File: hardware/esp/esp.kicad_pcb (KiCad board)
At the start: 2 copper layers, 100 x 80 mm, 7 parts, among them J1 USB_C_Receptacle_USB2.0_16P, U1 BME280, U2 VL53L0X, U3 NRF24L01, U4 ESP32-S3-WROOM-1, U5 NT3H1101W0FHK

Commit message: Updating PCb and esp board schematics
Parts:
- removed the U3 at (114.0, 140.1)
- added C1: 10nF, Capacitor_SMD:C_0603_1608Metric, F.Cu at (170.9, 89.4)
- added C11: 1pF, Capacitor_SMD:C_0603_1608Metric, F.Cu at (181.9, 91.7)
- added C12: 0.1µF, Capacitor_SMD:C_0805_2012Metric, F.Cu at (148.3, 135.9)
- added C13: C, Capacitor_SMD:C_0603_1608Metric, F.Cu at (98.2, 86.0)
- added C14: 100nF, Capacitor_SMD:C_0603_1608Metric, F.Cu at (115.4, 138.5)
- added C15: C, Capacitor_SMD:C_0603_1608Metric, F.Cu at (91.8, 89.0)
- added C16: 4.7pF, Capacitor_SMD:C_0603_1608Metric, F.Cu at (103.2, 141.5)
- added C2: 1nF, Capacitor_SMD:C_0603_1608Metric, F.Cu at (162.9, 100.7)
- added C3: 33nF, Capacitor_SMD:C_0603_1608Metric, F.Cu at (167.9, 102.7)
- added C4: 22pF, Capacitor_SMD:C_0603_1608Metric, F.Cu at (175.9, 110.2)
- added C5: 2.2pF, Capacitor_SMD:C_0603_1608Metric, F.Cu at (176.9, 103.7)
- added C7: 22pF, Capacitor_SMD:C_0603_1608Metric, F.Cu at (182.9, 103.7)
- added C8: 4.7pF, Capacitor_SMD:C_0603_1608Metric, F.Cu at (176.9, 90.4)
- added C9: 1.5pF, Capacitor_SMD:C_0603_1608Metric, F.Cu at (180.9, 80.4)
- added L2: 8.2nH, Inductor_SMD:L_0603_1608Metric, F.Cu at (168.9, 83.4)
- added L3: 2.7nH, Inductor_SMD:L_0603_1608Metric, F.Cu at (171.4, 83.4)
- added L4: 2.7nH, Inductor_SMD:L_0603_1608Metric, F.Cu at (173.9, 83.4)
- added R10: 10K, Resistor_SMD:R_0805_2012Metric, F.Cu at (148.3, 132.9)
- added R16: 1.5K, Resistor_SMD:R_0805_2012Metric, F.Cu at (108.1, 142.5)
- added R17: 1.5K, Resistor_SMD:R_0805_2012Metric, F.Cu at (105.2, 132.5)
- added R18: 1.5K, Resistor_SMD:R_0805_2012Metric, F.Cu at (102.2, 136.5)
- added R19: R, Resistor_SMD:R_0805_2012Metric, F.Cu at (101.9, 80.0)
- added R20: 1.5K, Resistor_SMD:R_0805_2012Metric, F.Cu at (113.1, 131.5)
- added R21: R, Resistor_SMD:R_0805_2012Metric, F.Cu at (88.0, 76.0)
- added R22: R, Resistor_SMD:R_0805_2012Metric, F.Cu at (96.1, 74.0)
- added R3: 22K, Resistor_SMD:R_0603_1608Metric, F.Cu at (168.9, 108.6)
- added R4: 22R, Resistor_SMD:R_0805_2012Metric, F.Cu at (96.9, 118.0)
- added R5: 22R, Resistor_SMD:R_0805_2012Metric, F.Cu at (103.0, 122.0)
- added R6: 5.1k, Resistor_SMD:R_0805_2012Metric, F.Cu at (103.1, 117.0)
- added R7: 5.1k, Resistor_SMD:R_0805_2012Metric, F.Cu at (97.0, 123.0)
- added R8: 1M, Resistor_SMD:R_0805_2012Metric, F.Cu at (180.9, 115.3)
- added R9: 10k, Resistor_SMD:R_0805_2012Metric, F.Cu at (148.3, 130.0)
- added SW1: RESET, Button_Switch_SMD:SW_SPST_SKQG_WithStem, F.Cu at (107.0, 97.0)
- added SW2: BOOT, Button_Switch_SMD:SW_SPST_SKQG_WithStem, F.Cu at (155.0, 116.0)
- added U2: NRF24L01, Package_DFN_QFN:QFN-20-1EP_4x4mm_P0.5mm_EP2.5x2.5mm, F.Cu at (168.9, 97.5)
- added Y1: 16MHz, Crystal:Crystal_SMD_3225-4Pin_3.2x2.5mm, F.Cu at (175.9, 97.4)
- moved U4 60.0 mm to (109.8, 137.0)
- moved J1 8.89 mm to (88.0, 120.1)
- renumbered U5 to U1, U4 to U3, U2 to U4, U1 to U5
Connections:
- J1 pad A5: unconnected-(J1-CC1-PadA5) -> Net-(J1-CC1)
- J1 pad B5: unconnected-(J1-CC2-PadB5) -> Net-(J1-CC2)
- U1 pad 2: unconnected-(U5-VSS-Pad2) -> GND
- U1 pad 3: unconnected-(U5-SCL-Pad3) -> SCL
- U1 pad 4: unconnected-(U5-FD-Pad4) -> NFC_FD
- U1 pad 5: unconnected-(U5-SDA-Pad5) -> SDA
- U1 pad 6: unconnected-(U5-VCC-Pad6) -> +3V3
- U3 pad 1: Net-(U4-GND-Pad1) -> GND
- U3 pad 12: unconnected-(U4-IO8-Pad12) -> SDA
- U3 pad 15: unconnected-(U4-IO3-Pad15) -> C.SKULL
- U3 pad 17: unconnected-(U4-IO9-Pad17) -> SCL
- U3 pad 2: unconnected-(U4-3V3-Pad2) -> +3V3
- U3 pad 27: unconnected-(U4-IO0-Pad27) -> BOOT
- U3 pad 3: unconnected-(U4-EN-Pad3) -> EN
- U3 pad 38: unconnected-(U4-IO2-Pad38) -> O.SKULL
- U3 pad 39: unconnected-(U4-IO1-Pad39) -> NRFLED
- U3 pad 4: unconnected-(U4-IO4-Pad4) -> NF.SKULL
- U3 pad 40: Net-(U4-GND-Pad1) -> GND
- U3 pad 41: Net-(U4-GND-Pad1) -> GND
- U3 pad 5: unconnected-(U4-IO5-Pad5) -> NFCLED
- U4 pad 1: unconnected-(U2-AVDDVCSEL-Pad1) -> +3V3
- U4 pad 10: unconnected-(U2-SCL-Pad10) -> SCL
- U4 pad 11: unconnected-(U2-AVDD-Pad11) -> +3V3
- U4 pad 2: unconnected-(U2-AVSSVCSEL-Pad2) -> GND
- U4 pad 5: unconnected-(U2-~{XSHUT}-Pad5) -> XSHUT
- U4 pad 7: unconnected-(U2-GPIO1-Pad7) -> DIST_GPIO1
- U4 pad 9: unconnected-(U2-SDA-Pad9) -> SDA
- U5 pad 1: unconnected-(U1-GND-Pad1) -> GND
- U5 pad 2: unconnected-(U1-CSB-Pad2) -> Net-(U5-CSB)
- U5 pad 3: unconnected-(U1-SDI-Pad3) -> SDA
- U5 pad 4: unconnected-(U1-SCK-Pad4) -> SCL
- U5 pad 6: unconnected-(U1-VDDIO-Pad6) -> +3V3
- U5 pad 7: unconnected-(U1-GND-Pad7) -> GND
- U5 pad 8: unconnected-(U1-VDD-Pad8) -> +3V3

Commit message: Updating schematics and PCB
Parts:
- removed L4: 2.7nH, Inductor_SMD:L_0603_1608Metric
- added C10: 33nF, Capacitor_SMD:C_0603_1608Metric, F.Cu at (34.0, 146.4)
- added C17: 1.5pF, Capacitor_SMD:C_0603_1608Metric, F.Cu at (38.0, 148.9)
- added C18: 1pF, Capacitor_SMD:C_0603_1608Metric, F.Cu at (38.0, 151.4)
- added C19: C, Capacitor_SMD:C_0603_1608Metric, F.Cu at (38.0, 154.0)
- added C20: C, Capacitor_SMD:C_0603_1608Metric, F.Cu at (42.0, 141.4)
- added C6: 0.1µF, Capacitor_SMD:C_0805_2012Metric, F.Cu at (29.7, 136.1)
- added D1: LED, LED_SMD:LED_0603_1608Metric, F.Cu at (63.3, 120.8)
- added D2: LED, LED_SMD:LED_0603_1608Metric, F.Cu at (63.3, 123.4)
- added D3: LED, LED_SMD:LED_0603_1608Metric, F.Cu at (63.3, 126.0)
- added D4: LED, LED_SMD:LED_0603_1608Metric, F.Cu at (63.3, 128.6)
- added D5: LED, LED_SMD:LED_0603_1608Metric, F.Cu at (63.3, 131.2)
- added D6: LED, LED_SMD:LED_0603_1608Metric, F.Cu at (63.3, 133.7)
- added D7: LED, LED_SMD:LED_0603_1608Metric, F.Cu at (63.3, 136.3)
- added G***: LOGO, LOGO, F.Cu at (179.0, 133.0)
- added G***: LOGO, LOGO, F.Cu at (169.0, 141.0)
- added J2: Conn_01x02, Connector_PinHeader_2.54mm:PinHeader_1x02_P2.54mm_Vertical, F.Cu at (139.0, 72.5)
- added J3: USB_C_Receptacle_USB2.0_16P, Connector_USB:USB_C_Receptacle_HCTL_HC-TYPE-C-16P-01A, F.Cu at (101.7, 72.1)
- added J4: Conn_01x01_Pin, Connector_PinHeader_1.00mm:PinHeader_1x01_P1.00mm_Vertical, F.Cu at (98.0, 116.0)
- added J5: Conn_01x09_Pin, Connector_PinHeader_2.54mm:PinHeader_1x09_P2.54mm_Vertical, F.Cu at (91.7, 105.0)
- added J6: Conn_01x09_Pin, Connector_PinHeader_2.54mm:PinHeader_1x09_P2.54mm_Vertical, F.Cu at (158.9, 105.0)
- added L1: 8.2nH, Inductor_SMD:L_0603_1608Metric, F.Cu at (42.0, 143.9)
- added R1: 22R, Resistor_SMD:R_0805_2012Metric, F.Cu at (34.2, 121.0)
- added R11: R, Resistor_SMD:R_0805_2012Metric, F.Cu at (38.6, 129.8)
- added R12: R, Resistor_SMD:R_0805_2012Metric, F.Cu at (38.6, 132.8)
- added R13: R, Resistor_SMD:R_0805_2012Metric, F.Cu at (38.6, 135.7)
- added R14: 1.5K, Resistor_SMD:R_0805_2012Metric, F.Cu at (38.6, 138.7)
- added R15: 1.5K, Resistor_SMD:R_0805_2012Metric, F.Cu at (43.0, 121.0)
- added R2: 22R, Resistor_SMD:R_0805_2012Metric, F.Cu at (34.2, 123.9)
- added R23: 22R, Resistor_SMD:R_0805_2012Metric, F.Cu at (47.4, 121.0)
- added R24: 22R, Resistor_SMD:R_0805_2012Metric, F.Cu at (47.4, 123.9)
- added R25: 5.1k, Resistor_SMD:R_0805_2012Metric, F.Cu at (47.4, 126.9)
- added R26: 5.1k, Resistor_SMD:R_0805_2012Metric, F.Cu at (47.4, 129.8)
- added U6: CP2102N-Axx-xQFN20, Package_DFN_QFN:SiliconLabs_QFN-20-1EP_3x3mm_P0.5mm_EP1.8x1.8mm, F.Cu at (101.8, 88.8)
- C1: value 10nF -> 10uF; footprint Capacitor_SMD:C_0603_1608Metric -> Capacitor_SMD:C_0805_2012Metric
- C11: value 1pF -> 100nF
- C12: value 0.1µF -> 22pF; footprint Capacitor_SMD:C_0805_2012Metric -> Capacitor_SMD:C_0603_1608Metric
- C13: value C -> 2.2pF
- C14: value 100nF -> 4.7pF
- C15: value C -> 22pF
- C2: value 1nF -> 0.1uF; footprint Capacitor_SMD:C_0603_1608Metric -> Capacitor_SMD:C_0805_2012Metric
- C3: value 33nF -> 10uF; footprint Capacitor_SMD:C_0603_1608Metric -> Capacitor_SMD:C_0805_2012Metric
- C4: value 22pF -> 0.1uF; footprint Capacitor_SMD:C_0603_1608Metric -> Capacitor_SMD:C_0805_2012Metric
- C5: value 2.2pF -> C; footprint Capacitor_SMD:C_0603_1608Metric -> Capacitor_SMD:C_0805_2012Metric
- C7: value 22pF -> C; footprint Capacitor_SMD:C_0603_1608Metric -> Capacitor_SMD:C_0805_2012Metric
- C8: value 4.7pF -> 10nF
- C9: value 1.5pF -> 1nF
- L2: value 8.2nH -> 2.7nH
- R10: value 10K -> R
- R16: value 1.5K -> 22K; footprint Resistor_SMD:R_0805_2012Metric -> Resistor_SMD:R_0603_1608Metric
- R19: value R -> 1M
- R20: value 1.5K -> R
- R3: value 22K -> 5.1k; footprint Resistor_SMD:R_0603_1608Metric -> Resistor_SMD:R_0805_2012Metric
- R4: value 22R -> 5.1k
- R5: value 22R -> R
- R6: value 5.1k -> 10k
- R7: value 5.1k -> 10K
- R8: value 1M -> R
- R9: value 10k -> R
- U1: value NT3H1101W0FHK -> AMS1117-3.3; footprint NT3H1101W0FHK:IC_NT3H1101W0FHK -> Package_TO_SOT_SMD:SOT-223-3_TabPin2
- U2: value NRF24L01 -> ESP32-S3-WROOM-1; footprint Package_DFN_QFN:QFN-20-1EP_4x4mm_P0.5mm_EP2.5x2.5mm -> RF_Module:ESP32-S3-WROOM-1
- U3: value ESP32-S3-WROOM-1 -> VL53L0X; footprint RF_Module:ESP32-S3-WROOM-1 -> VL53L0X:SENSOR_VL53L0X
- U4: value VL53L0X -> NRF24L01; footprint VL53L0X:SENSOR_VL53L0X -> Package_DFN_QFN:QFN-20-1EP_4x4mm_P0.5mm_EP2.5x2.5mm
- moved C9 160.1 mm to (34.0, 143.9), turned to 0 degrees
- moved C11 158.7 mm to (34.0, 148.9), turned to 0 degrees
- moved C7 157.2 mm to (29.7, 139.1), turned to 0 degrees
- moved C8 151.8 mm to (34.0, 141.4), turned to 0 degrees
- moved C5 150.1 mm to (29.7, 133.0), turned to 0 degrees
- moved C4 147.6 mm to (29.7, 130.0), turned to 0 degrees
- moved L3 145.1 mm to (42.0, 148.9), turned to 0 degrees
- moved C1 144.7 mm to (29.7, 121.0), turned to 0 degrees
- moved R8 142.5 mm to (38.6, 121.0), turned to 0 degrees
- moved L2 141.7 mm to (42.0, 146.4), turned to 0 degrees
- moved C3 140.3 mm to (29.7, 127.0), turned to 0 degrees
- moved R3 136.0 mm to (34.2, 126.9), turned to 0 degrees
- moved C2 135.2 mm to (29.7, 124.0), turned to 0 degrees
- moved C12 115.4 mm to (34.0, 151.4)
- moved R10 109.9 mm to (38.6, 126.9)
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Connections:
- C1 pad 1: GND -> +5V
- C1 pad 2: +3V3 -> GND
- C11 pad 1: GND -> +3V3
- C11 pad 2: Net-(C11-Pad2) -> GND
- C12 pad 2: EN -> Net-(U4-XC1)
- C13 pad 1: GND -> Net-(U4-VDD_PA)
- C13 pad 2: +3V3 -> GND
- C15 pad 1: +3V3 -> Net-(U4-XC2)
- C16 pad 1: +3V3 -> Net-(U4-VDD_PA)
- C2 pad 1: GND -> +5V
- C2 pad 2: +3V3 -> GND
- C3 pad 1: Net-(U2-DVDD) -> +3V3
- C4 pad 1: GND -> +3V3
- C4 pad 2: Net-(U2-XC1) -> GND
- C5 pad 1: Net-(U2-VDD_PA) -> GND
- C5 pad 2: GND -> +3V3
- C7 pad 1: Net-(U2-XC2) -> GND
- C7 pad 2: GND -> +3V3
- C8 pad 1: Net-(U2-VDD_PA) -> GND
- C8 pad 2: GND -> +3V3
- C9 pad 1: Net-(C9-Pad1) -> GND
- C9 pad 2: Net-(C11-Pad2) -> +3V3
- L2 pad 1: Net-(U2-ANT2) -> Net-(U4-ANT2)
- L2 pad 2: Net-(U2-ANT1) -> Net-(C17-Pad1)
- L3 pad 1: Net-(U2-ANT2) -> Net-(U4-ANT1)
- L3 pad 2: Net-(C9-Pad1) -> Net-(U4-VDD_PA)
- R10 pad 1: +3V3 -> NRFLED
- R10 pad 2: BOOT -> Net-(D4-A)
- R16 pad 1: +3V3 -> GND
- R16 pad 2: SDA -> Net-(U4-IREF)
- R17 pad 2: SCL -> XSHUT
- R18 pad 2: XSHUT -> DIST_GPIO1
- R19 pad 1: +3V3 -> Net-(U4-XC1)
- R19 pad 2: SDA -> Net-(U4-XC2)
- R20 pad 2: DIST_GPIO1 -> SDA
- R3 pad 1: GND -> Net-(J1-CC1)
- R3 pad 2: Net-(U2-IREF) -> GND
- R4 pad 1: Net-(J1-D--PadA7) -> Net-(J1-CC2)
- R4 pad 2: D- -> GND
- R5 pad 1: Net-(J1-D+-PadA6) -> Net-(D1-A)
- R5 pad 2: D+ -> +3V3
- R6 pad 1: Net-(J1-CC1) -> EN
- R6 pad 2: GND -> +3V3
- R7 pad 1: Net-(J1-CC2) -> +3V3
- R7 pad 2: GND -> BOOT
- R8 pad 1: Net-(U2-XC1) -> unconnected-(R8-Pad1)
- R8 pad 2: Net-(U2-XC2) -> Net-(D2-A)
- R9 pad 1: EN -> unconnected-(R9-Pad1)
- R9 pad 2: +3V3 -> Net-(D3-A)
- U1 pad 1: Net-(U1-LA) -> GND
- U1 pad 2: GND -> +3V3
- U1 pad 3: SCL -> +5V
- U2 pad 1: NRF_CE -> GND
- U2 pad 10: Net-(U2-XC1) -> unconnected-(U2-IO17-Pad10)
- U2 pad 11: Net-(U2-VDD_PA) -> unconnected-(U2-IO18-Pad11)
- U2 pad 12: Net-(U2-ANT1) -> SDA
- U2 pad 13: Net-(U2-ANT2) -> D-
- U2 pad 14: GND -> D+
- U2 pad 15: +3V3 -> C.SKULL
- U2 pad 16: Net-(U2-IREF) -> unconnected-(U2-IO46-Pad16)
- U2 pad 17: GND -> SCL
- U2 pad 18: +3V3 -> unconnected-(U2-IO10-Pad18)
- U2 pad 19: Net-(U2-DVDD) -> unconnected-(U2-IO11-Pad19)
- U2 pad 2: NRF_CSN -> +3V3
- U2 pad 21: (no net) -> unconnected-(U2-IO13-Pad21)
- U2 pad 3: SPI_SCK -> EN
- U2 pad 4: SPI_MOSI -> NF.SKULL
- U2 pad 5: SPI_MISO -> NFCLED
- U2 pad 7: +3V3 -> unconnected-(U2-IO7-Pad7)
- U2 pad 8: GND -> unconnected-(U2-IO15-Pad8)
- U2 pad 9: Net-(U2-XC2) -> unconnected-(U2-IO16-Pad9)
- U3 pad 1: GND -> +3V3
- U3 pad 10: unconnected-(U3-IO17-Pad10) -> SCL
- U3 pad 11: unconnected-(U3-IO18-Pad11) -> +3V3
- U3 pad 12: SDA -> GND
- U3 pad 2: +3V3 -> GND
- U3 pad 3: EN -> GND
- U3 pad 4: NF.SKULL -> GND
- U3 pad 5: NFCLED -> XSHUT
- U3 pad 6: unconnected-(U3-IO6-Pad6) -> GND
- U3 pad 7: unconnected-(U3-IO7-Pad7) -> DIST_GPIO1
- U3 pad 8: unconnected-(U3-IO15-Pad8) -> (no net)
- U3 pad 9: unconnected-(U3-IO16-Pad9) -> SDA
- U4 pad 1: +3V3 -> NRF_CE
- U4 pad 10: SCL -> Net-(U4-XC1)
- U4 pad 11: +3V3 -> Net-(U4-VDD_PA)
- U4 pad 12: GND -> Net-(U4-ANT1)
- U4 pad 2: GND -> NRF_CSN
- U4 pad 3: GND -> SPI_SCK
- U4 pad 4: GND -> SPI_MOSI
- U4 pad 5: XSHUT -> SPI_MISO
- U4 pad 6: GND -> unconnected-(U4-IRQ-Pad6)
- U4 pad 7: DIST_GPIO1 -> +3V3
- U4 pad 8: (no net) -> GND
- U4 pad 9: SDA -> Net-(U4-XC2)
- Y1 pad 1: Net-(U2-XC2) -> Net-(U4-XC2)
- Y1 pad 3: Net-(U2-XC1) -> Net-(U4-XC1)
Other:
- board text added: "@OZane"
- board text added: "E.L.B.E.R.R. Fanmade"
- board text added: "no copper"

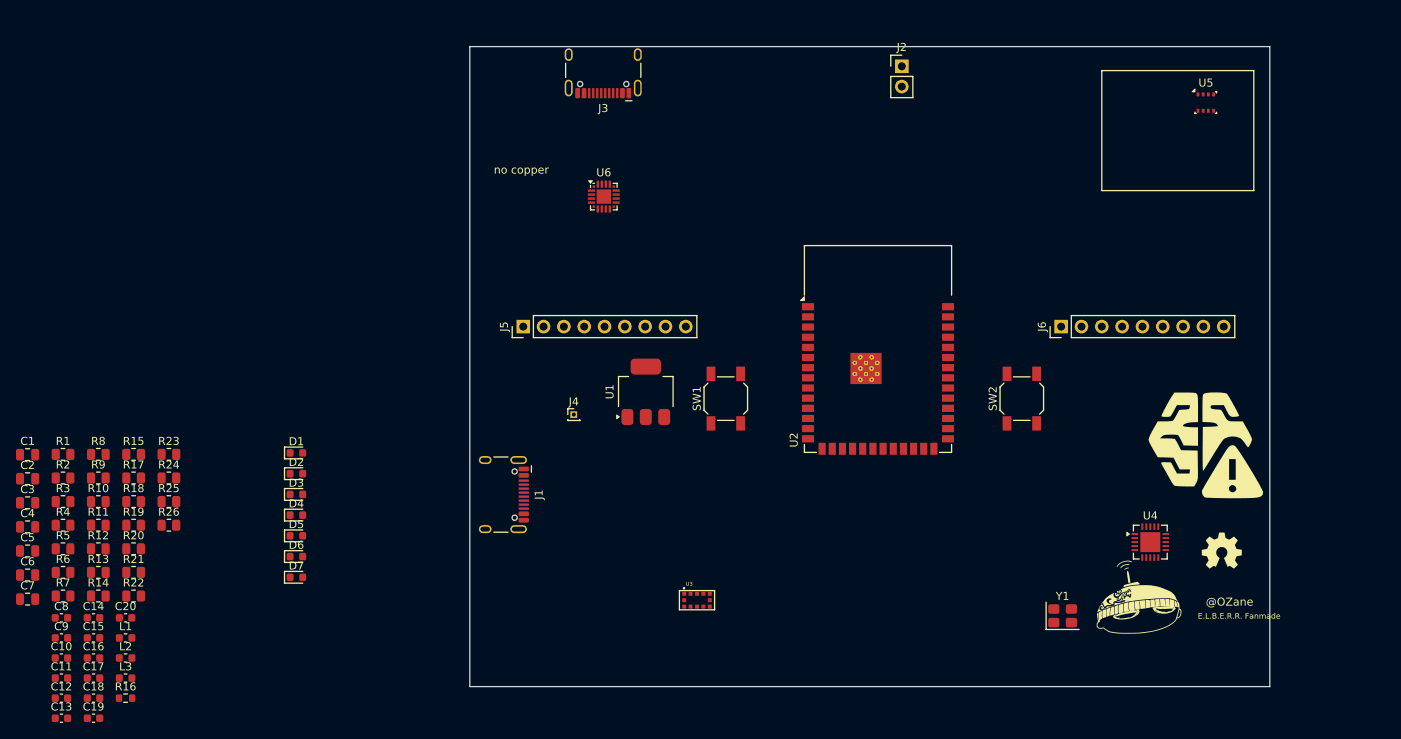
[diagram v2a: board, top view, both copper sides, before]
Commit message: Updating pins, working on schematic and placing components on PCB
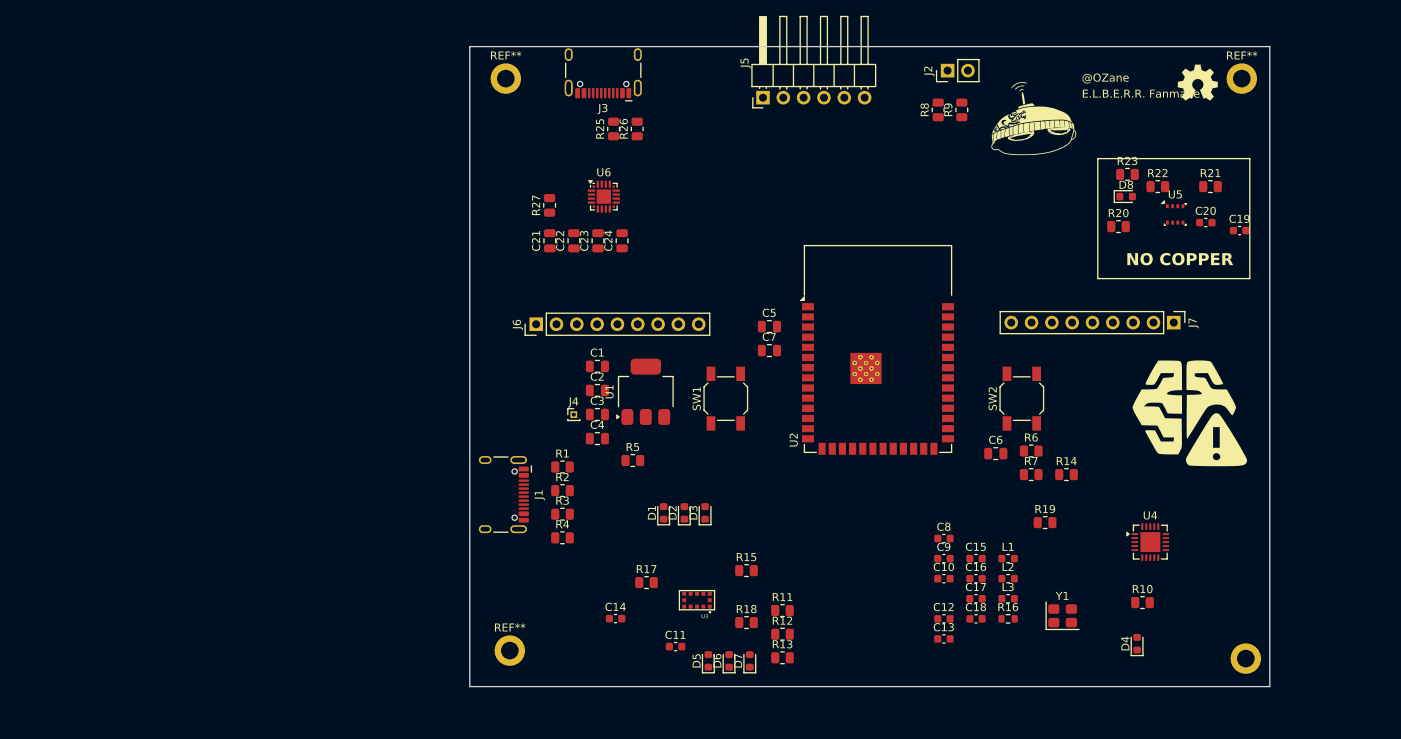
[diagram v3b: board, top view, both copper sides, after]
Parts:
- removed R24: 22R, Resistor_SMD:R_0805_2012Metric
- added C21: 0.1uF, Capacitor_SMD:C_0805_2012Metric, F.Cu at (95.0, 94.3)
- added C22: 4.7uF, Capacitor_SMD:C_0805_2012Metric, F.Cu at (98.0, 94.3)
- added C23: 0.1uF, Capacitor_SMD:C_0805_2012Metric, F.Cu at (101.0, 94.3)
- added C24: 4.7uF, Capacitor_SMD:C_0805_2012Metric, F.Cu at (104.0, 94.3)
- added D8: LED, LED_SMD:LED_0603_1608Metric, F.Cu at (167.0, 88.7)
- added J7: Conn_01x09_Pin, Connector_PinHeader_2.54mm:PinHeader_1x09_P2.54mm_Vertical, F.Cu at (173.0, 104.5)
- added R27: 1k, Resistor_SMD:R_0805_2012Metric, F.Cu at (95.0, 89.8)
- added REF**: MountingHole_2.2mm_M2_DIN965_Pad, MountingHole:MountingHole_2.2mm_M2_DIN965_Pad, F.Cu at (89.5, 74.0)
- added REF**: MountingHole_2.2mm_M2_DIN965_Pad, MountingHole:MountingHole_2.2mm_M2_DIN965_Pad, F.Cu at (90.0, 145.5)
- added REF**: MountingHole_2.2mm_M2_DIN965_Pad, MountingHole:MountingHole_2.2mm_M2_DIN965_Pad, F.Cu at (181.5, 74.0)
- added REF**: MountingHole_2.2mm_M2_DIN965_Pad, MountingHole:MountingHole_2.2mm_M2_DIN965_Pad, F.Cu at (182.0, 146.5)
- J5: value Conn_01x09_Pin -> Conn_01x06_Pin; footprint Connector_PinHeader_2.54mm:PinHeader_1x09_P2.54mm_Vertical -> Connector_PinHeader_2.54mm:PinHeader_1x06_P2.54mm_Horizontal
- R23: value 22R -> R
- moved C19 155.7 mm to (181.2, 93.0)
- moved C20 143.8 mm to (177.0, 92.0)
- moved R21 143.0 mm to (177.6, 87.5)
- moved R22 137.9 mm to (171.0, 87.5)
- moved R10 131.1 mm to (169.1, 139.5)
- moved R20 129.5 mm to (166.1, 92.5)
- moved R23 124.8 mm to (167.2, 86.0)
- moved C6 122.0 mm to (150.7, 120.9)
- moved R14 122.0 mm to (159.6, 123.5)
- moved R6 122.0 mm to (155.2, 120.5)
- moved R7 122.0 mm to (155.2, 123.5)
- moved R9 117.3 mm to (146.5, 77.9), turned to 90 degrees
- moved R19 113.9 mm to (156.9, 129.5)
- moved R8 113.5 mm to (143.6, 77.9), turned to 90 degrees
- moved C15 110.8 mm to (148.3, 134.0)
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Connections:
- net NFCLED renamed TX_LED
- J3 pad A4: +5V -> Net-(U6-VBUS)
- J3 pad A6: Net-(J3-D+-PadA6) -> Net-(U6-D+)
- J3 pad A7: Net-(J3-D--PadA7) -> Net-(U6-D-)
- J3 pad A9: +5V -> Net-(U6-VBUS)
- J3 pad B4: +5V -> Net-(U6-VBUS)
- J3 pad B6: Net-(J3-D+-PadA6) -> Net-(U6-D+)
- J3 pad B7: Net-(J3-D--PadA7) -> Net-(U6-D-)
- J3 pad B9: +5V -> Net-(U6-VBUS)
- J5 pad 1: unconnected-(J5-Pin_1-Pad1) -> LP
- J5 pad 2: +5V -> LV
- J5 pad 3: GND -> LH
- J5 pad 4: unconnected-(J5-Pin_4-Pad4) -> RH
- J5 pad 5: +5V -> RV
- J5 pad 6: GND -> RH
- J6 pad 1: unconnected-(J6-Pin_1-Pad1) -> LH
- J6 pad 4: unconnected-(J6-Pin_4-Pad4) -> LV
- J6 pad 7: unconnected-(J6-Pin_7-Pad7) -> LP
- R23 pad 1: Net-(J3-D--PadA7) -> TEMP_LED
- R23 pad 2: D- -> Net-(D8-A)
- U2 pad 10: unconnected-(U2-IO17-Pad10) -> TX2
- U2 pad 11: unconnected-(U2-IO18-Pad11) -> RX2
- U2 pad 18: unconnected-(U2-IO10-Pad18) -> NRF_CSN
- U2 pad 19: unconnected-(U2-IO11-Pad19) -> MOSI
- U2 pad 20: unconnected-(U2-IO12-Pad20) -> SCK
- U2 pad 21: unconnected-(U2-IO13-Pad21) -> MISO
- U2 pad 22: unconnected-(U2-IO14-Pad22) -> NRF_CE
- U2 pad 6: unconnected-(U2-IO6-Pad6) -> RX_LED
- U2 pad 7: unconnected-(U2-IO7-Pad7) -> TEMP_LED
- U6 pad 12: Net-(U6-GND-Pad12) -> GND
- U6 pad 17: unconnected-(U6-RXD-Pad17) -> TX2
- U6 pad 18: unconnected-(U6-TXD-Pad18) -> RX2
- U6 pad 21: Net-(U6-GND-Pad12) -> GND
- U6 pad 3: Net-(U6-GND-Pad12) -> GND
- U6 pad 4: unconnected-(U6-D+-Pad4) -> Net-(U6-D+)
- U6 pad 5: unconnected-(U6-D--Pad5) -> Net-(U6-D-)
- U6 pad 6: unconnected-(U6-VDD-Pad6) -> +3V3
- U6 pad 8: unconnected-(U6-VBUS-Pad8) -> Net-(U6-VBUS)
- U6 pad 9: unconnected-(U6-~{RST}-Pad9) -> Net-(U6-~{RST})
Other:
- board text added: "DISTANCE SENSOR"
- board text added: "NO COPPER"
- board text added: "NRF24"
- board text removed: "no copper"

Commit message: Updating schematics and PCB layout
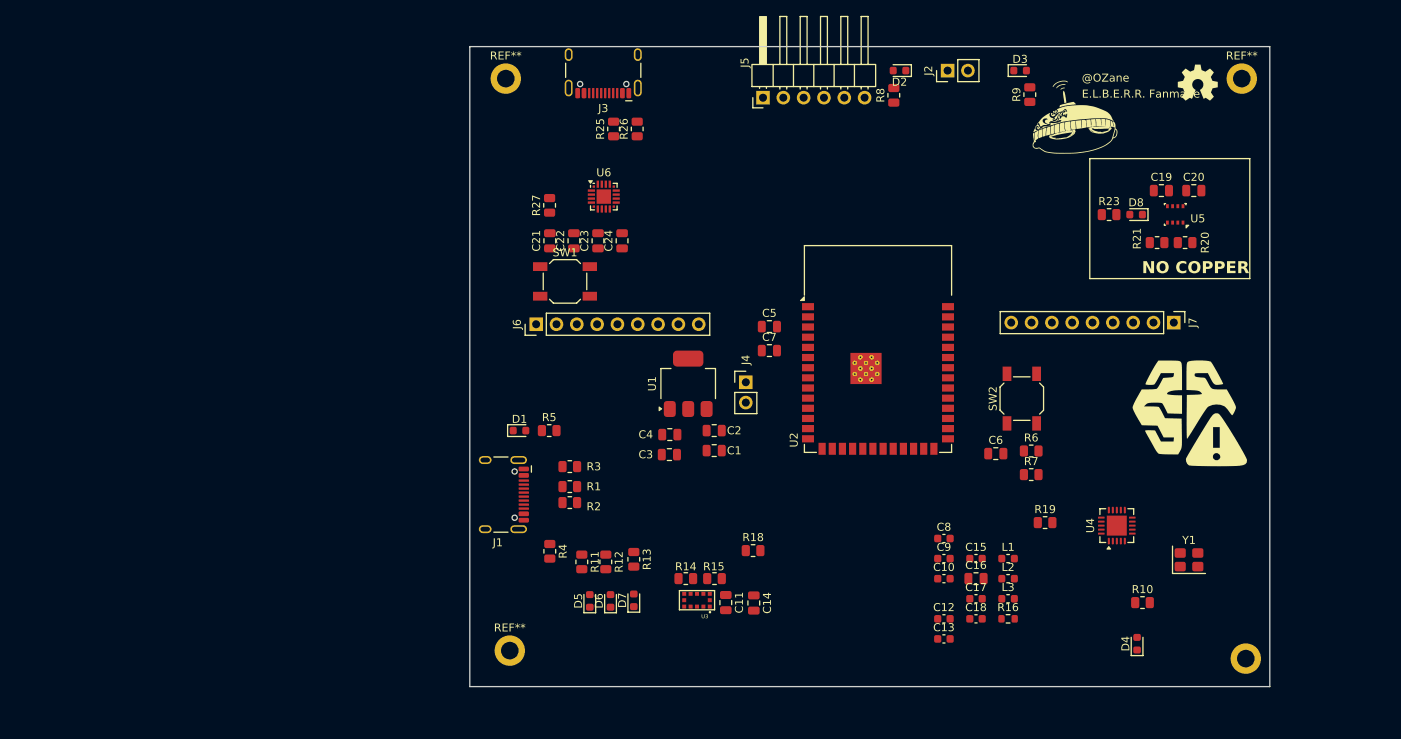
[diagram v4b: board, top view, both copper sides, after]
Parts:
- removed R17: 1.5K, Resistor_SMD:R_0805_2012Metric
- removed R22: R, Resistor_SMD:R_0805_2012Metric
- C11, C14, C16: footprint Capacitor_SMD:C_0603_1608Metric -> Capacitor_SMD:C_0805_2012Metric
- C19, C20: value C -> 0.1uF; footprint Capacitor_SMD:C_0603_1608Metric -> Capacitor_SMD:C_0805_2012Metric
- C5: value C -> 100uF
- C7: value C -> 10uF
- J4: value Conn_01x01_Pin -> Conn_01x02; footprint Connector_PinHeader_1.00mm:PinHeader_1x01_P1.00mm_Vertical -> Connector_PinHeader_2.54mm:PinHeader_1x02_P2.54mm_Vertical
- R14, R15: value 1.5K -> 4.7k
- R20, R21: value R -> 4.7k
- moved D3 67.9 mm to (153.8, 73.0), turned to 0 degrees
- moved D2 61.5 mm to (138.7, 73.0), turned to 180 degrees
- moved R14 49.3 mm to (112.0, 136.5)
- moved R11 25.8 mm to (99.0, 134.4), turned to -90 degrees
- moved SW1 24.9 mm to (96.9, 99.4), turned to 0 degrees
- moved R12 23.9 mm to (102.0, 134.4), turned to -90 degrees
- moved R13 22.3 mm to (105.5, 134.1), turned to -90 degrees
- moved J4 21.9 mm to (119.5, 112.0)
- moved D1 20.7 mm to (91.2, 118.0), turned to 0 degrees
- moved C1 18.0 mm to (115.5, 120.5)
- moved C14 17.4 mm to (120.5, 139.6), turned to -90 degrees
- moved Y1 17.3 mm to (174.9, 134.2)
- moved D5 16.6 mm to (100.0, 139.3)
- moved D6 16.6 mm to (102.6, 139.3)
- moved D7 16.4 mm to (105.5, 139.2)
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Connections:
- D2 pad 1: unconnected-(D2-K-Pad1) -> GND
- D3 pad 1: unconnected-(D3-K-Pad1) -> GND
- J2 pad 1: UART_STX -> RX2
- J2 pad 2: UART_SRX -> TX2
- J4 pad 1: +5V -> GND
- R8 pad 1: unconnected-(R8-Pad1) -> RX_LED
- R9 pad 1: unconnected-(R9-Pad1) -> TX_LED
- U3 pad 5: XSHUT -> +3V3
- U3 pad 7: DIST_GPIO1 -> unconnected-(U3-GPIO1-Pad7)
- U5 pad 2: Net-(U5-CSB) -> +3V3
- U6 pad 7: unconnected-(U6-VREGIN-Pad7) -> Net-(U6-VBUS)
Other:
- board text added: "RX"
- board text added: "TX"
